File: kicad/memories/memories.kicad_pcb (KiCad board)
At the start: 2 copper layers, 59.9 x 64.3 mm, 39 parts, among them J1 DB15_Female_HighDensity, J3 DIN-6, U1 NAND512, U2 AMS1117-3V3, U3 MT48LC32M8A2

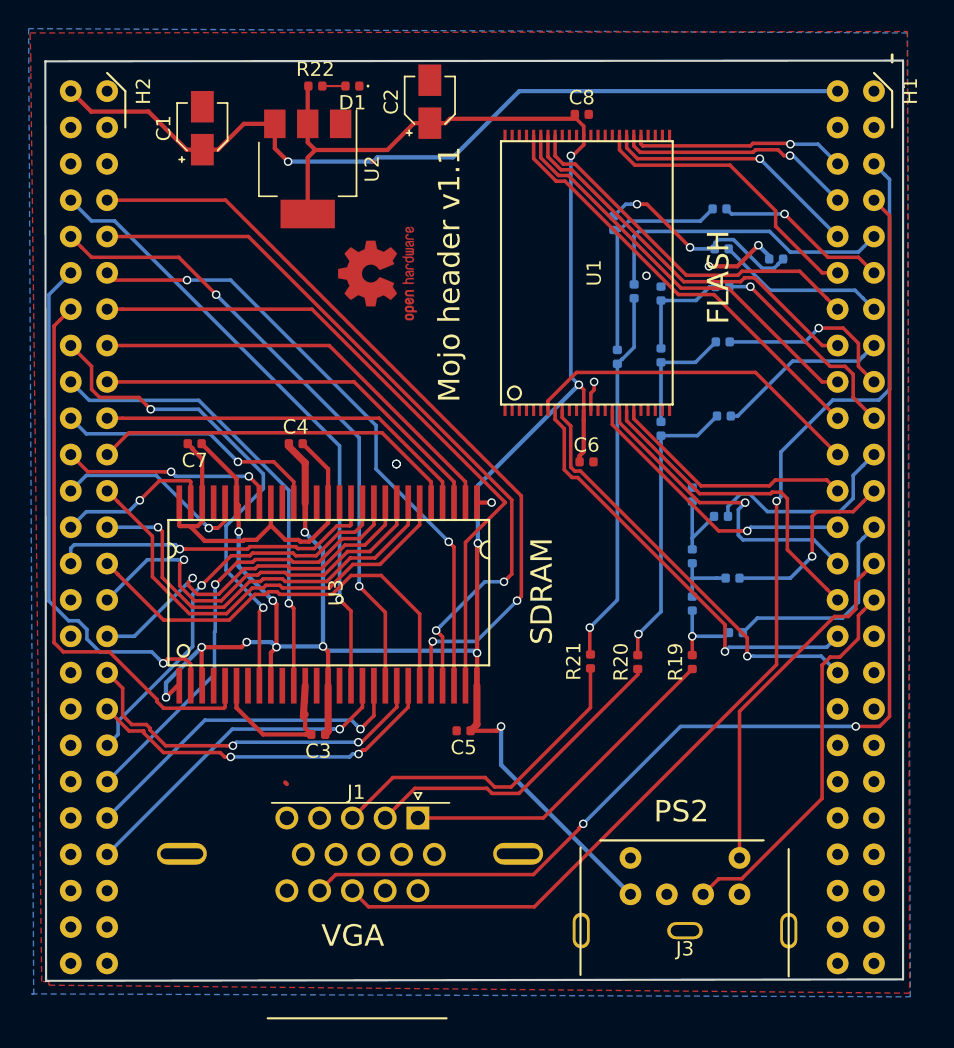
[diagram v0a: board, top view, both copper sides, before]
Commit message: kicad: enlarged footprint for capacitor 0402 for hand soldering.
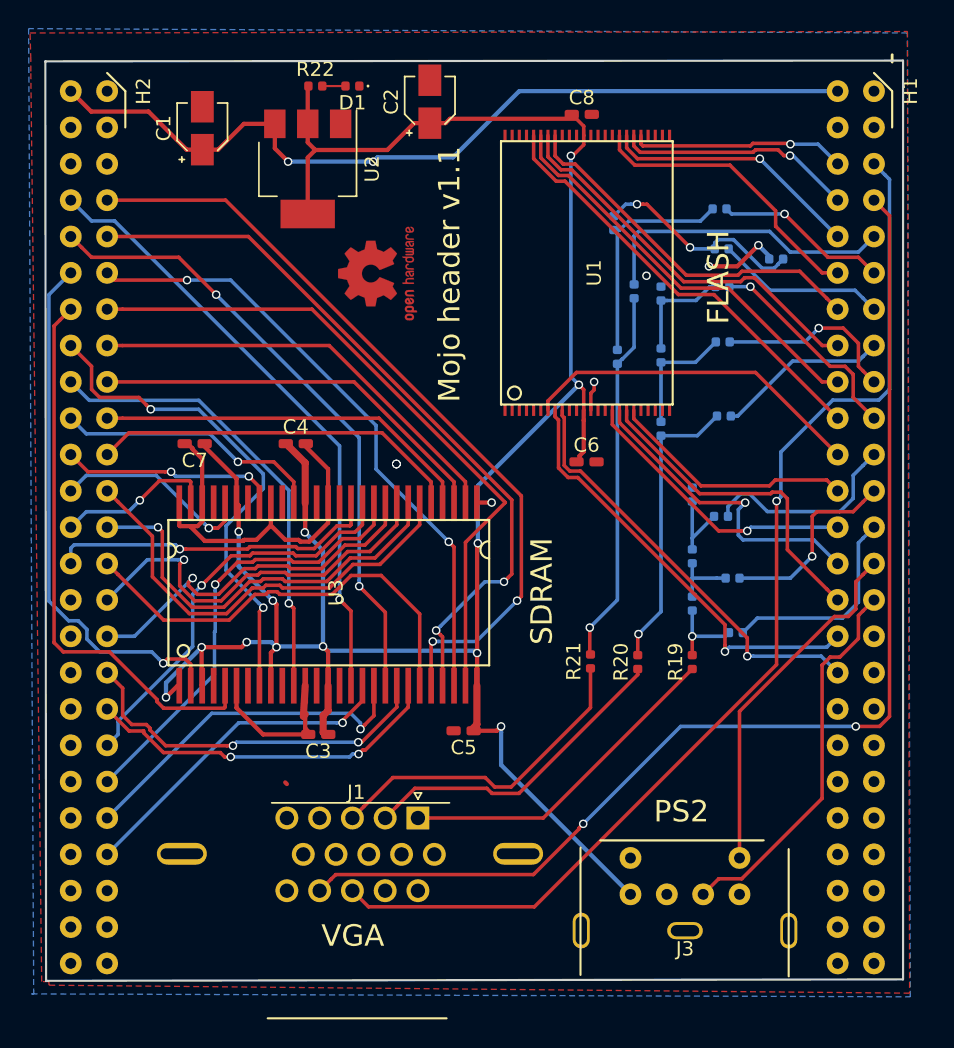
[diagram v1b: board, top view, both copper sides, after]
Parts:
- C3, C4, C5, C6, C7, C8: footprint Capacitor_SMD:C_0402_1005Metric -> Capacitor_SMD:C_0402_handSoldering
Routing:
- net Net-(H2-Pad21): track 24.2 -> 24.9 mm
- net V_EXTERNAL: vias 1 -> 2

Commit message: kicad/memories/pcb: fix R-2R ladder labels.
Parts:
- R1, R10, R11, R12, R16, R17, R18, R2, R3, R4, R5, R6: value R -> 560
- R13, R14, R15, R7, R8, R9: value R -> 270
- R19, R20, R21: value R -> 0
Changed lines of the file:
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@@
       (effects (font (size 1 1) (thickness 0.15)) (justify mirror))
     )
-    (fp_text value R (at 0 -1.17 180) (layer B.Fab)
+    (fp_text value 560 (at 0 -1.17 180) (layer B.Fab)
       (effects (font (size 1 1) (thickness 0.15)) (justify mirror))
     )
@@
     (tags resistor)
     (attr smd)
-    (fp_text reference R2 (at 0 1.17 90) (layer B.SilkS)
-      (effects (font (size 1 1) (thickness 0.15)) (justify mirror))
-    )
-    (fp_text value R (at 0 -1.17 90) (layer B.Fab)
+    (fp_text reference R2 (at 0.0508 -1.1684 90) (layer B.SilkS)
+      (effects (font (size 1 1) (thickness 0.15)) (justify mirror))
+    )
+    (fp_text value 560 (at 0.1016 -2.54 90) (layer B.Fab)
       (effects (font (size 1 1) (thickness 0.15)) (justify mirror))
     )
@@
       (effects (font (size 1 1) (thickness 0.15)) (justify mirror))
     )
-    (fp_text value R (at 0 -1.17 180) (layer B.Fab)
+    (fp_text value 560 (at 0 -1.17 180) (layer B.Fab)
       (effects (font (size 1 1) (thickness 0.15)) (justify mirror))
     )
@@
       (effects (font (size 1 1) (thickness 0.15)) (justify mirror))
     )
-    (fp_text value R (at 0 -1.17 90) (layer B.Fab)
+    (fp_text value 560 (at 0 -1.17 90) (layer B.Fab)
       (effects (font (size 1 1) (thickness 0.15)) (justify mirror))
     )
@@
     (tags resistor)
     (attr smd)
-    (fp_text reference R5 (at 0 1.17 270) (layer B.SilkS)
-      (effects (font (size 1 1) (thickness 0.15)) (justify mirror))
-    )
-    (fp_text value R (at 0 -1.17 180) (layer B.Fab)
+    (fp_text reference R5 (at 0 1.17) (layer B.SilkS)
+      (effects (font (size 1 1) (thickness 0.15)) (justify mirror))
+    )
+    (fp_text value 560 (at 0 -1.17 180) (layer B.Fab)
       (effects (font (size 1 1) (thickness 0.15)) (justify mirror))
     )
@@
       (effects (font (size 1 1) (thickness 0.15)) (justify mirror))
     )
-    (fp_text value R (at 0 -1.17 180) (layer B.Fab)
+    (fp_text value 560 (at 0 -1.17 180) (layer B.Fab)
       (effects (font (size 1 1) (thickness 0.15)) (justify mirror))
     )
@@
     (tags resistor)
     (attr smd)
-    (fp_text reference R7 (at 0 1.17 90) (layer B.SilkS)
-      (effects (font (size 1 1) (thickness 0.15)) (justify mirror))
-    )
-    (fp_text value R (at 0 -1.17 90) (layer B.Fab)
+    (fp_text reference R7 (at -0.0508 -1.0668 90) (layer B.SilkS)
+      (effects (font (size 1 1) (thickness 0.15)) (justify mirror))
+    )
+    (fp_text value 270 (at -0.1016 -2.3368 90) (layer B.Fab)
       (effects (font (size 1 1) (thickness 0.15)) (justify mirror))
     )
@@
       (effects (font (size 1 1) (thickness 0.15)) (justify mirror))
     )
-    (fp_text value R (at 0 -1.17 180) (layer B.Fab)
+    (fp_text value 270 (at 0 -1.17 270) (layer B.Fab)
       (effects (font (size 1 1) (thickness 0.15)) (justify mirror))
     )
@@
       (effects (font (size 1 1) (thickness 0.15)) (justify mirror))
     )
-    (fp_text value R (at 0 -1.17 90) (layer B.Fab)
+    (fp_text value 270 (at 0 -1.17 90) (layer B.Fab)
       (effects (font (size 1 1) (thickness 0.15)) (justify mirror))
     )
@@
       (effects (font (size 1 1) (thickness 0.15)) (justify mirror))
     )
-    (fp_text value R (at 0 -1.17 180) (layer B.Fab)
+    (fp_text value 560 (at 0 -1.17 180) (layer B.Fab)
       (effects (font (size 1 1) (thickness 0.15)) (justify mirror))
     )
@@
       (effects (font (size 1 1) (thickness 0.15)) (justify mirror))
     )
-    (fp_text value R (at 0 -1.17 180) (layer B.Fab)
+    (fp_text value 560 (at 0 -1.17 180) (layer B.Fab)
       (effects (font (size 1 1) (thickness 0.15)) (justify mirror))
     )
@@
     (tags resistor)
     (attr smd)
-    (fp_text reference R12 (at 0 1.17 270) (layer B.SilkS)
-      (effects (font (size 1 1) (thickness 0.15)) (justify mirror))
-    )
-    (fp_text value R (at 0 -1.17 180) (layer B.Fab)
+    (fp_text reference R12 (at 0 1.17) (layer B.SilkS)
+      (effects (font (size 1 1) (thickness 0.15)) (justify mirror))
+    )
+    (fp_text value 560 (at 0 -1.17 180) (layer B.Fab)
       (effects (font (size 1 1) (thickness 0.15)) (justify mirror))
     )
@@
     (tags resistor)
     (attr smd)
-    (fp_text reference R13 (at 0 1.17 90) (layer B.SilkS)
-      (effects (font (size 1 1) (thickness 0.15)) (justify mirror))
-    )
-    (fp_text value R (at 0 -1.17 90) (layer B.Fab)
+    (fp_text reference R13 (at 0.0508 -1.2192 90) (layer B.SilkS)
+      (effects (font (size 1 1) (thickness 0.15)) (justify mirror))
+    )
+    (fp_text value 270 (at 0.1016 -2.4384 90) (layer B.Fab)
       (effects (font (size 1 1) (thickness 0.15)) (justify mirror))
     )
@@
       (effects (font (size 1 1) (thickness 0.15)) (justify mirror))
     )
-    (fp_text value R (at 0 -1.17 90) (layer B.Fab)
+    (fp_text value 270 (at 0 -1.17 90) (layer B.Fab)
       (effects (font (size 1 1) (thickness 0.15)) (justify mirror))
     )
@@
       (effects (font (size 1 1) (thickness 0.15)) (justify mirror))
     )
-    (fp_text value R (at 0 -1.17 90) (layer B.Fab)
+    (fp_text value 270 (at 0 -1.17 90) (layer B.Fab)
       (effects (font (size 1 1) (thickness 0.15)) (justify mirror))
     )
@@
       (effects (font (size 1 1) (thickness 0.15)) (justify mirror))
     )
-    (fp_text value R (at 0 -1.17 180) (layer B.Fab)
+    (fp_text value 560 (at 0 -1.17 180) (layer B.Fab)
       (effects (font (size 1 1) (thickness 0.15)) (justify mirror))
     )
@@
       (effects (font (size 1 1) (thickness 0.15)) (justify mirror))
     )
-    (fp_text value R (at 0 -1.17 180) (layer B.Fab)
+    (fp_text value 560 (at 0 -1.17 180) (layer B.Fab)
       (effects (font (size 1 1) (thickness 0.15)) (justify mirror))
     )
@@
       (effects (font (size 1 1) (thickness 0.15)) (justify mirror))
     )
-    (fp_text value R (at 0 -1.17 270) (layer B.Fab)
+    (fp_text value 560 (at 0 -1.17 270) (layer B.Fab)
       (effects (font (size 1 1) (thickness 0.15)) (justify mirror))
     )
@@
       (effects (font (size 1 1) (thickness 0.15)))
     )
-    (fp_text value R (at 0 1.17 90) (layer F.Fab)
+    (fp_text value 0 (at 0 1.17 90) (layer F.Fab)
       (effects (font (size 1 1) (thickness 0.15)))
     )
@@
       (effects (font (size 1 1) (thickness 0.15)))
     )
-    (fp_text value R (at 0 1.17 90) (layer F.Fab)
+    (fp_text value 0 (at 0 1.17 90) (layer F.Fab)
       (effects (font (size 1 1) (thickness 0.15)))
     )
@@
       (effects (font (size 1 1) (thickness 0.15)))
     )
-    (fp_text value R (at 0 1.17 90) (layer F.Fab)
+    (fp_text value 0 (at 0 1.17 90) (layer F.Fab)
       (effects (font (size 1 1) (thickness 0.15)))
     )
